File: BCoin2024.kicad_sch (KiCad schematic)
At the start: 20 parts, among them U1 NE555DR, U2 74HC4017D_653

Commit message: added datasheets
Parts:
- R1, R2, R3, R4: footprint Resistor_SMD:R_1206_3216Metric -> Resistor_SMD:R_0603_1608Metric
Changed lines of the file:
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@@
 		(title "BurbSec Challenge Coin 2024")
 		(date "2024-12-09")
-		(rev "0.1")
+		(rev "0.2")
 		(comment 1 "Email: youngd24@gmail.com")
 		(comment 2 "Author: DY")
@@
 			)
 		)
-		(property "Footprint" "Resistor_SMD:R_1206_3216Metric"
+		(property "Footprint" "Resistor_SMD:R_0603_1608Metric"
 			(at 84.582 78.74 90)
 			(effects
@@
 			)
 		)
-		(property "Datasheet" "~"
+		(property "Datasheet" "https://mm.digikey.com/Volume0/opasdata/d220001/medias/docus/39/RC_Series_ds.pdf"
 			(at 86.36 78.74 0)
 			(effects
@@
 			)
 		)
-		(property "Footprint" "Resistor_SMD:R_1206_3216Metric"
+		(property "Footprint" "Resistor_SMD:R_0603_1608Metric"
 			(at 212.09 133.858 90)
 			(effects
@@
 			)
 		)
-		(property "Datasheet" "~"
+		(property "Datasheet" "https://mm.digikey.com/Volume0/opasdata/d220001/medias/docus/39/RC_Series_ds.pdf"
 			(at 212.09 132.08 0)
 			(effects
@@
 			)
 		)
-		(property "Datasheet" "~"
+		(property "Datasheet" "https://mm.digikey.com/Volume0/opasdata/d220001/medias/docus/609/CL21A106KOQNNNE_Spec.pdf"
 			(at 86.36 119.38 0)
 			(effects
@@
 			)
 		)
-		(property "Footprint" "Resistor_SMD:R_1206_3216Metric"
+		(property "Footprint" "Resistor_SMD:R_0603_1608Metric"
 			(at 84.582 97.79 90)
 			(effects
@@
 			)
 		)
-		(property "Datasheet" "~"
+		(property "Datasheet" "https://mm.digikey.com/Volume0/opasdata/d220001/medias/docus/39/RC_Series_ds.pdf"
 			(at 86.36 97.79 0)
 			(effects
@@
 			)
 		)
-		(property "Footprint" "Resistor_SMD:R_1206_3216Metric"
+		(property "Footprint" "Resistor_SMD:R_0603_1608Metric"
 			(at 145.542 116.84 90)
 			(effects
@@
 			)
 		)
-		(property "Datasheet" "~"
+		(property "Datasheet" "https://mm.digikey.com/Volume0/opasdata/d220001/medias/docus/39/RC_Series_ds.pdf"
 			(at 147.32 116.84 0)
 			(effects
@@
 			)
 		)
-		(property "Datasheet" "~"
+		(property "Datasheet" "https://mm.digikey.com/Volume0/opasdata/d220001/medias/docus/5458/CL10B103KO8WPNC_Spec.pdf"
 			(at 124.46 119.38 0)
 			(effects

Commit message: Version 0.3
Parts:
- added C3: 10nF, Capacitor_SMD:C_0603_1608Metric, symbol Device:C
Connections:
- net GND: now also C3.2
- net VCC: now also C3.1
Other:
- title: BurbSec Challenge Coin 2024 -> BurbSec Meetup Coin 2024
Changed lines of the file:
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@@
 	(paper "USLetter")
 	(title_block
-		(title "BurbSec Challenge Coin 2024")
-		(date "2024-12-09")
-		(rev "0.2")
+		(title "BurbSec Meetup Coin 2024")
+		(date "2024-12-10")
+		(rev "0.3")
 		(comment 1 "Email: youngd24@gmail.com")
 		(comment 2 "Author: DY")
@@
 	)
 	(junction
+		(at 121.92 77.47)
+		(diameter 0)
+		(color 0 0 0 0)
+	)
+	(junction
 		(at 233.68 121.92)
 		(diameter 0)
@@
 	(wire
 		(pts
+			(xy 121.92 77.47) (xy 121.92 81.28)
+		)
+		(stroke
+			(width 0)
+			(type default)
+		)
+	)
+	(wire
+		(pts
 			(xy 210.82 93.98) (xy 210.82 91.44)
 		)
@@
 	(wire
 		(pts
-			(xy 121.92 67.31) (xy 121.92 81.28)
+			(xy 121.92 67.31) (xy 121.92 77.47)
 		)
 		(stroke
@@
 		(pts
 			(xy 115.57 67.31) (xy 115.57 81.28)
+		)
+		(stroke
+			(width 0)
+			(type default)
+		)
+	)
+	(wire
+		(pts
+			(xy 129.54 77.47) (xy 130.81 77.47)
 		)
 		(stroke
@@
 	)
 	(symbol
+		(lib_id "power:GND")
+		(at 130.81 77.47 90)
+		(unit 1)
+		(exclude_from_sim no)
+		(in_bom yes)
+		(on_board yes)
+		(dnp no)
+		(fields_autoplaced yes)
+		(property "Reference" "#PWR03"
+			(at 137.16 77.47 0)
+			(effects
+				(font
+					(size 1.27 1.27)
+				)
+				(hide yes)
+			)
+		)
+		(property "Value" "GND"
+			(at 134.62 77.4699 90)
+			(effects
+				(font
+					(size 1.27 1.27)
+				)
+				(justify right)
+			)
+		)
+		(property "Footprint" ""
+			(at 130.81 77.47 0)
+			(effects
+				(font
+					(size 1.27 1.27)
+				)
+				(hide yes)
+			)
+		)
+		(property "Datasheet" ""
+			(at 130.81 77.47 0)
+			(effects
+				(font
+					(size 1.27 1.27)
+				)
+				(hide yes)
+			)
+		)
+		(property "Description" "Power symbol creates a global label with name \"GND\" , ground"
+			(at 130.81 77.47 0)
+			(effects
+				(font
+					(size 1.27 1.27)
+				)
+				(hide yes)
+			)
+		)
+		(pin "1"
+		)
+		(instances
+			(project ""
+				(path "/81973eb7-292d-417c-8a8a-cb71070341da"
+					(reference "#PWR03")
+					(unit 1)
+				)
+			)
+		)
+	)
+	(symbol
 		(lib_id "Device:LED")
 		(at 226.06 106.68 180)
@@
 					(unit 1)
 				)
+			)
+		)
+	)
+	(symbol
+		(lib_id "Device:C")
+		(at 125.73 77.47 90)
+		(unit 1)
+		(exclude_from_sim no)
+		(in_bom yes)
+		(on_board yes)
+		(dnp no)
+		(property "Reference" "C3"
+			(at 125.476 71.628 90)
+			(effects
+				(font
+					(size 1.27 1.27)
+				)
+			)
+		)
+		(property "Value" "10nF"
+			(at 125.984 73.66 90)
+			(effects
+				(font
+					(size 1.27 1.27)
+				)
+			)
+		)
+		(property "Footprint" "Capacitor_SMD:C_0603_1608Metric"
+			(at 129.54 76.5048 0)
+			(effects
+				(font
+					(size 1.27 1.27)
+				)
+				(hide yes)
+			)
+		)
+		(property "Datasheet" "https://mm.digikey.com/Volume0/opasdata/d220001/medias/docus/5458/CL10B103KO8WPNC_Spec.pdf"
+			(at 125.73 77.47 0)
+			(effects
+				(font
+					(size 1.27 1.27)
+				)
+				(hide yes)
+			)
+		)
+		(property "Description" "Unpolarized capacitor"
+			(at 125.73 77.47 0)
+			(effects
+				(font
+					(size 1.27 1.27)
+				)
+				(hide yes)
+			)
+		)
+		(pin "2"
+		)
+		(pin "1"
+		)
+		(instances
+			(project "BCoin2024"
+				(path "/81973eb7-292d-417c-8a8a-cb71070341da"
+					(reference "C3")
+					(unit 1)
+				)

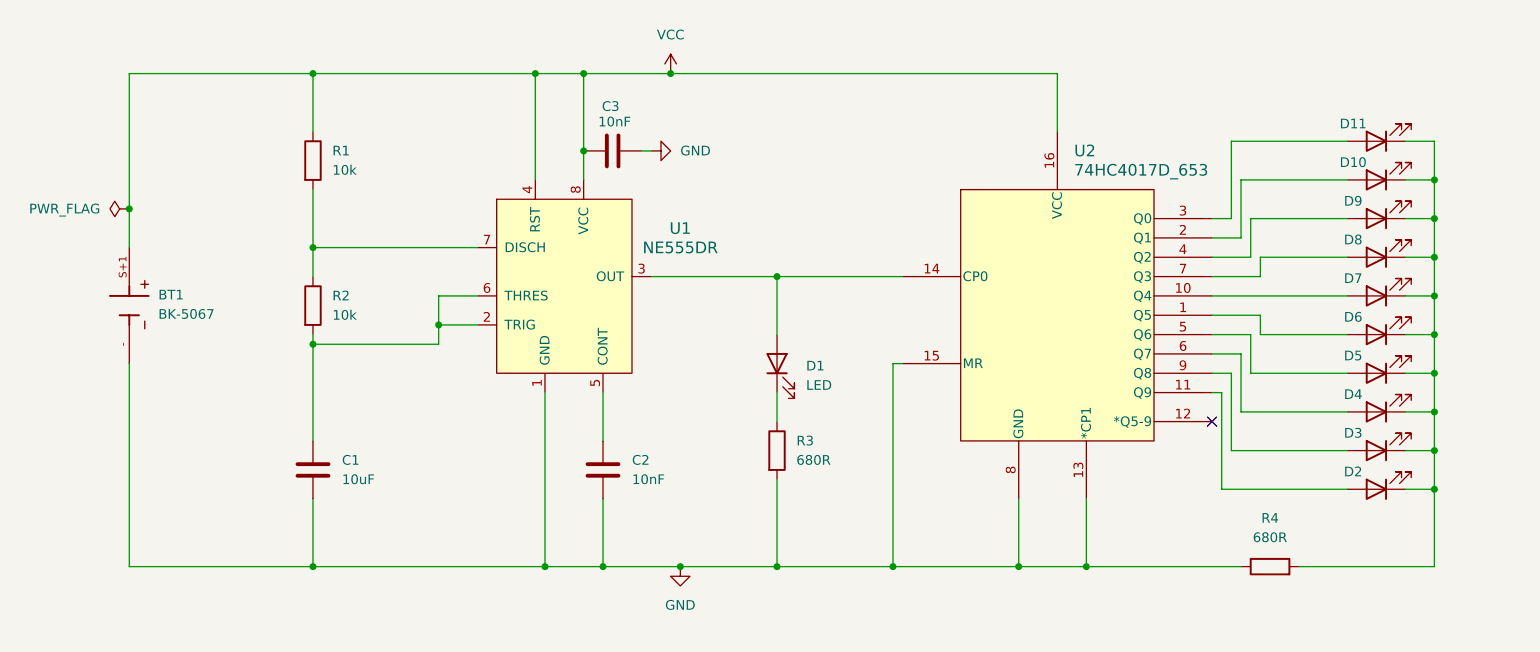
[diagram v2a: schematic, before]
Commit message: added updated 0.4 schematic
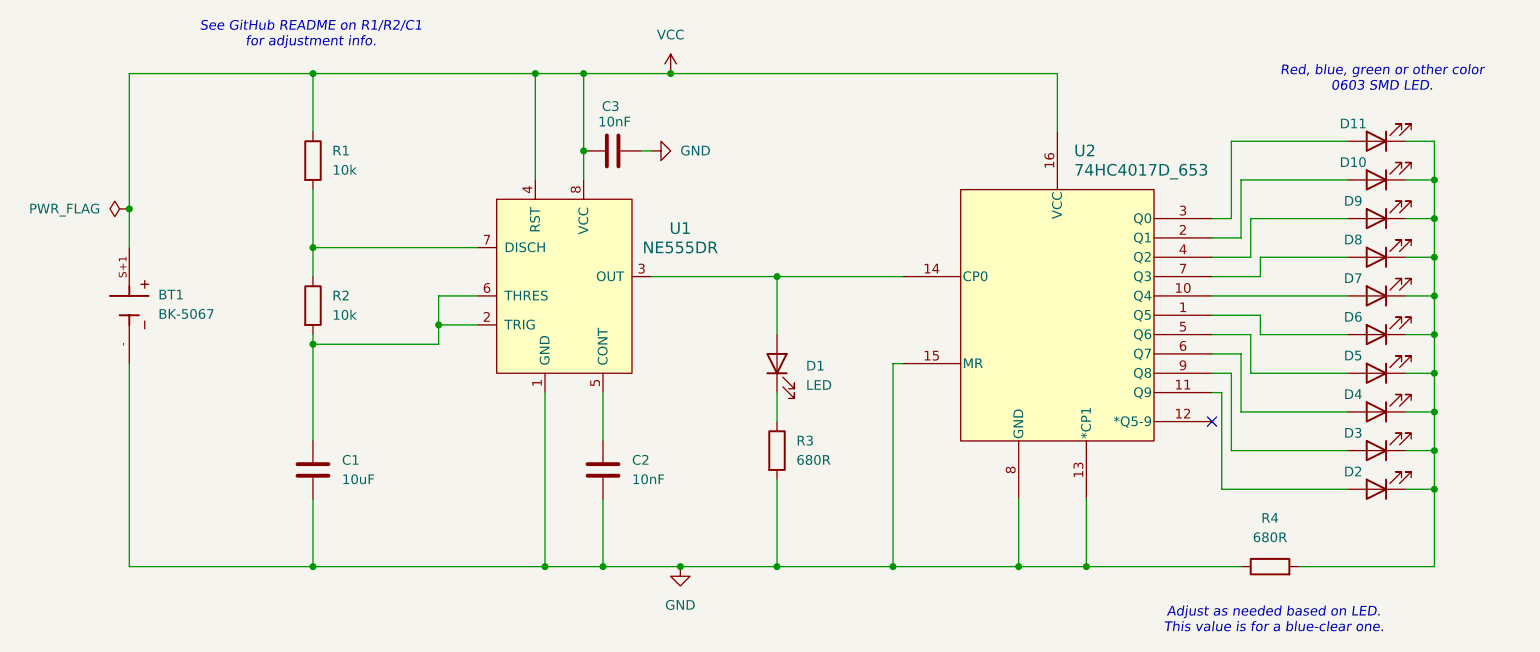
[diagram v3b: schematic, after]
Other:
- note added: "Adjust as needed based on LED. This value is for a blue-clear one."
- note added: "Red, blue, green or other color 0603 SMD LED."
- note added: "See GitHub README on R1/R2/C1 for adjustment info."
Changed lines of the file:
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@@
 	(title_block
 		(title "BurbSec Meetup Coin 2024")
-		(date "2024-12-10")
-		(rev "0.3")
+		(date "2024-12-20")
+		(rev "0.4")
 		(comment 1 "Email: youngd24@gmail.com")
 		(comment 2 "Author: DY")
@@
 		)
 	)
+	(text "Adjust as needed based on LED.\nThis value is for a blue-clear one."
+		(exclude_from_sim yes)
+		(at 212.598 139.192 0)
+		(effects
+			(font
+				(size 1.27 1.27)
+				(italic yes)
+			)
+		)
+	)
+	(text "Red, blue, green or other color\n0603 SMD LED."
+		(exclude_from_sim yes)
+		(at 226.822 68.072 0)
+		(effects
+			(font
+				(size 1.27 1.27)
+				(italic yes)
+			)
+		)
+	)
+	(text "See GitHub README on R1/R2/C1\nfor adjustment info."
+		(exclude_from_sim yes)
+		(at 86.106 62.23 0)
+		(effects
+			(font
+				(size 1.27 1.27)
+				(italic yes)
+			)
+		)
+	)

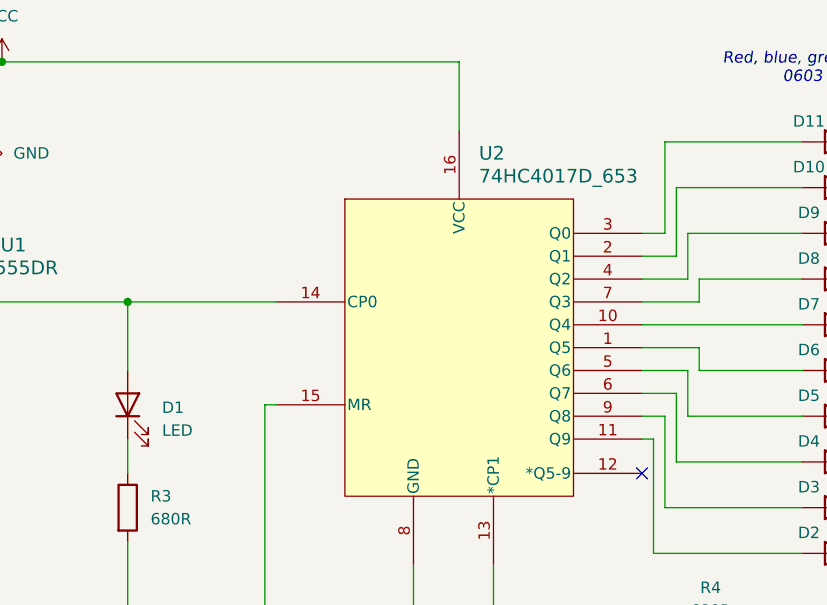
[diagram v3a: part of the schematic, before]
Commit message: added pcbway ignore and WayWayWay text for SN replacements
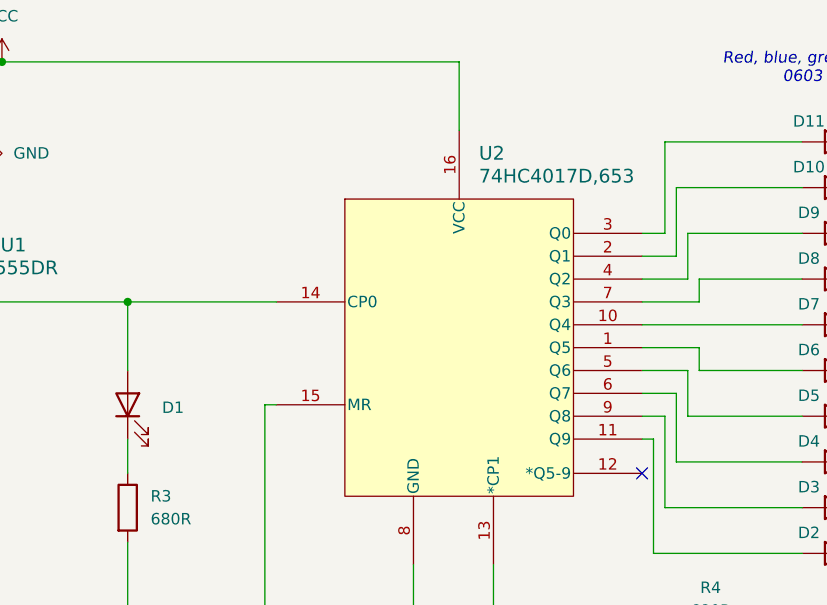
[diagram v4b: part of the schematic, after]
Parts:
- D1: value LED -> LED RED CLEAR 0603 SMD; MPN (none) -> 150060SS75000
- D10, D2, D3, D4, D5, D6, D7, D8, D9: value LED -> LED GREEN CLEAR 0603 SMD
- D11: value LED -> LED GREEN CLEAR 0603 SMD; MPN (none) -> 150060VS75000
- U2: value 74HC4017D_653 -> 74HC4017D,653
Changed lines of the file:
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@@
 			)
 		)
-		(property "Value" "74HC4017D_653"
+		(property "Value" "74HC4017D,653"
 			(at 186.3441 80.01 0)
 			(effects
@@
 			)
 		)
-		(property "Datasheet" "74HC4017D_653"
+		(property "Datasheet" "https://www.digikey.com/en/products/detail/nexperia-usa-inc/74HC4017D-653/1230369"
 			(at 169.926 80.518 0)
 			(effects
@@
 			)
 		)
-		(property "Description" ""
+		(property "Description" "IC DECADE COUNTER 10BIT 16SO"
 			(at 163.83 87.63 0)
 			(effects
@@
 			)
 		)
-		(property "Value" "LED"
+		(property "Value" "LED GREEN CLEAR 0603 SMD"
 			(at 226.06 108.712 0)
 			(effects
@@
 			)
 		)
-		(property "Datasheet" "~"
+		(property "Datasheet" "https://www.digikey.com/en/products/detail/w%C3%BCrth-elektronik/150060VS75000/4489906"
 			(at 226.06 111.76 0)
 			(effects
@@
 			)
 		)
-		(property "Value" "LED"
+		(property "Value" "LED GREEN CLEAR 0603 SMD"
 			(at 226.06 78.232 0)
 			(effects
@@
 			)
 		)
-		(property "Datasheet" "~"
+		(property "Datasheet" "https://www.digikey.com/en/products/detail/w%C3%BCrth-elektronik/150060VS75000/4489906"
 			(at 226.06 81.28 0)
 			(effects
@@
 	)
 	(symbol
+		(lib_name "LED_1")
 		(lib_id "Device:LED")
 		(at 226.06 76.2 180)
@@
 			)
 		)
-		(property "Value" "LED"
+		(property "Value" "LED GREEN CLEAR 0603 SMD"
 			(at 226.06 73.152 0)
 			(effects
@@
 			)
 		)
-		(property "Datasheet" "~"
+		(property "Datasheet" "https://www.digikey.com/en/products/detail/w%C3%BCrth-elektronik/150060VS75000/4489906"
 			(at 226.06 76.2 0)
 			(effects
@@
 			)
 		)
+		(property "MPN" "150060VS75000"
+			(at 226.06 76.2 0)
+			(effects
+				(font
+					(size 1.27 1.27)
+				)
+				(hide yes)
+			)
+		)
 		(pin "1"
 		)
@@
 			)
 		)
-		(property "Value" "LED"
+		(property "Value" "LED GREEN CLEAR 0603 SMD"
 			(at 226.06 113.792 0)
 			(effects
@@
 			)
 		)
-		(property "Datasheet" "~"
+		(property "Datasheet" "https://www.digikey.com/en/products/detail/w%C3%BCrth-elektronik/150060VS75000/4489906"
 			(at 226.06 116.84 0)
 			(effects
@@
 			)
 		)
-		(property "Value" "LED"
+		(property "Value" "LED GREEN CLEAR 0603 SMD"
 			(at 226.06 88.392 0)
 			(effects
@@
 			)
 		)
-		(property "Datasheet" "~"
+		(property "Datasheet" "https://www.digikey.com/en/products/detail/w%C3%BCrth-elektronik/150060VS75000/4489906"
 			(at 226.06 91.44 0)
 			(effects
@@
 	)
 	(symbol
+		(lib_name "R_1")
 		(lib_id "Device:R")
 		(at 212.09 132.08 90)
@@
 			)
 		)
-		(property "Value" "LED"
+		(property "Value" "LED GREEN CLEAR 0603 SMD"
 			(at 226.06 103.632 0)
 			(effects
@@
 			)
 		)
-		(property "Datasheet" "~"
+		(property "Datasheet" "https://www.digikey.com/en/products/detail/w%C3%BCrth-elektronik/150060VS75000/4489906"
 			(at 226.06 106.68 0)
 			(effects
@@
 			)
 		)
-		(property "Value" "LED"
+		(property "Value" "LED GREEN CLEAR 0603 SMD"
 			(at 226.06 98.552 0)
 			(effects
@@
 			)
 		)
-		(property "Datasheet" "~"
+		(property "Datasheet" "https://www.digikey.com/en/products/detail/w%C3%BCrth-elektronik/150060VS75000/4489906"
 			(at 226.06 101.6 0)
 			(effects
@@
 			)
 		)
-		(property "Value" "LED"
+		(property "Value" "LED GREEN CLEAR 0603 SMD"
 			(at 226.06 118.872 0)
 			(effects
@@
 			)
 		)
-		(property "Datasheet" "~"
+		(property "Datasheet" "https://www.digikey.com/en/products/detail/w%C3%BCrth-elektronik/150060VS75000/4489906"
 			(at 226.06 121.92 0)
 			(effects
@@
 			)
 		)
-		(property "Value" "LED"
+		(property "Value" "LED GREEN CLEAR 0603 SMD"
 			(at 226.06 93.472 0)
 			(effects
@@
 			)
 		)
-		(property "Datasheet" "~"
+		(property "Datasheet" "https://www.digikey.com/en/products/detail/w%C3%BCrth-elektronik/150060VS75000/4489906"
 			(at 226.06 96.52 0)
 			(effects
@@
 			)
 		)
-		(property "Value" "LED"
+		(property "Value" "LED RED CLEAR 0603 SMD"
 			(at 151.13 108.2674 90)
 			(effects
@@
 				)
 				(justify right)
+				(hide yes)
 			)
 		)
@@
 			)
 		)
-		(property "Datasheet" "~"
+		(property "Datasheet" "https://www.digikey.com/en/products/detail/w%C3%BCrth-elektronik/150060SS75000/4489903"
 			(at 147.32 105.41 0)
 			(effects
@@
 		(property "Description" "Light emitting diode"
 			(at 147.32 105.41 0)
+			(effects
+				(font
+					(size 1.27 1.27)
+				)
+				(hide yes)
+			)
+		)
+		(property "MPN" "150060SS75000"
+			(at 147.32 105.41 90)
 			(effects
 				(font
@@
 			)
 		)
-		(property "Value" "LED"
+		(property "Value" "LED GREEN CLEAR 0603 SMD"
 			(at 226.06 83.312 0)
 			(effects
@@
 			)
 		)
-		(property "Datasheet" "~"
+		(property "Datasheet" "https://www.digikey.com/en/products/detail/w%C3%BCrth-elektronik/150060VS75000/4489906"
 			(at 226.06 86.36 0)
 			(effects
